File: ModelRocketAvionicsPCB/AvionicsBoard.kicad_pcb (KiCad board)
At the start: 4 copper layers, 30 x 55 mm, 67 parts, among them P1 FTSH-105-01-F-DV, P2 USB_OTG, P3 JST-2, U1 TM4C123GH6PM, U10 PMOS, U3 LIS331, U4 L3GD20HTR, U5 MPL3115A2, U6 MCP73831, U7 MIC5219-3.3BM5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

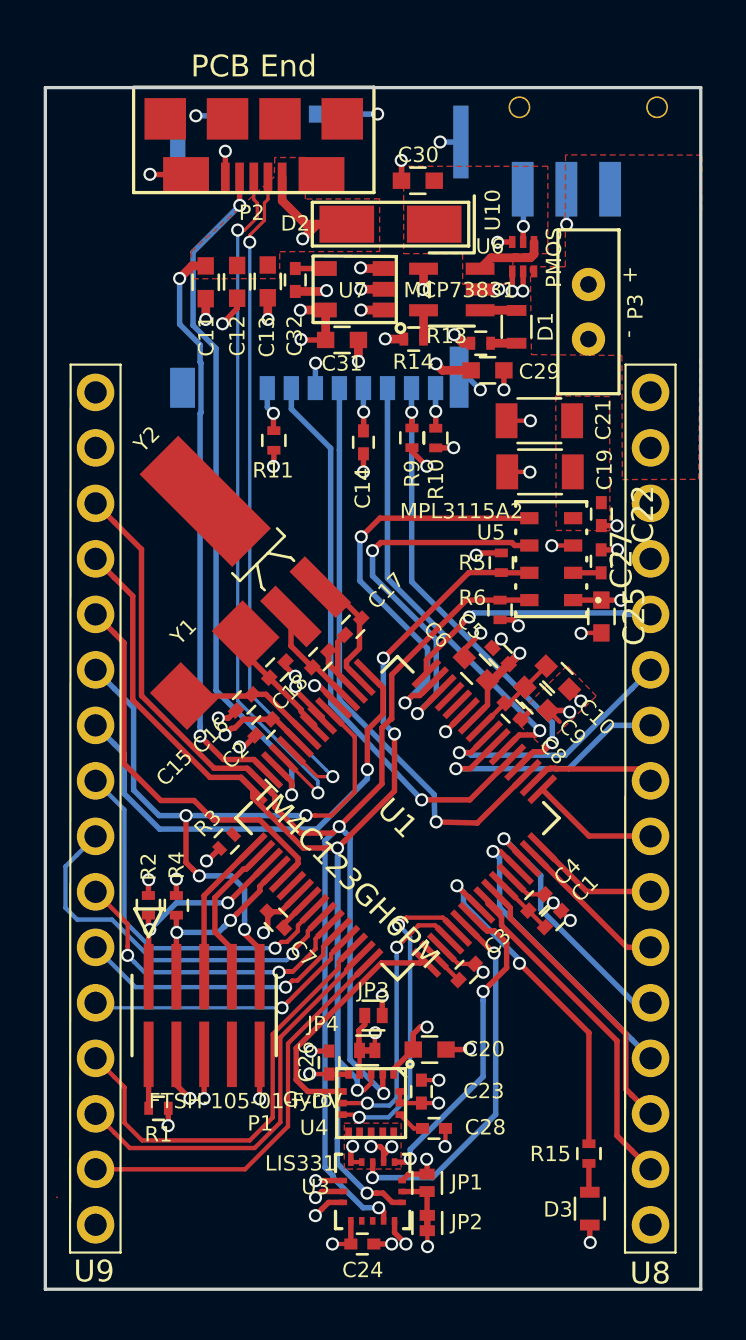
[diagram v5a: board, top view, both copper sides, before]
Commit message: DRC Issues Solved
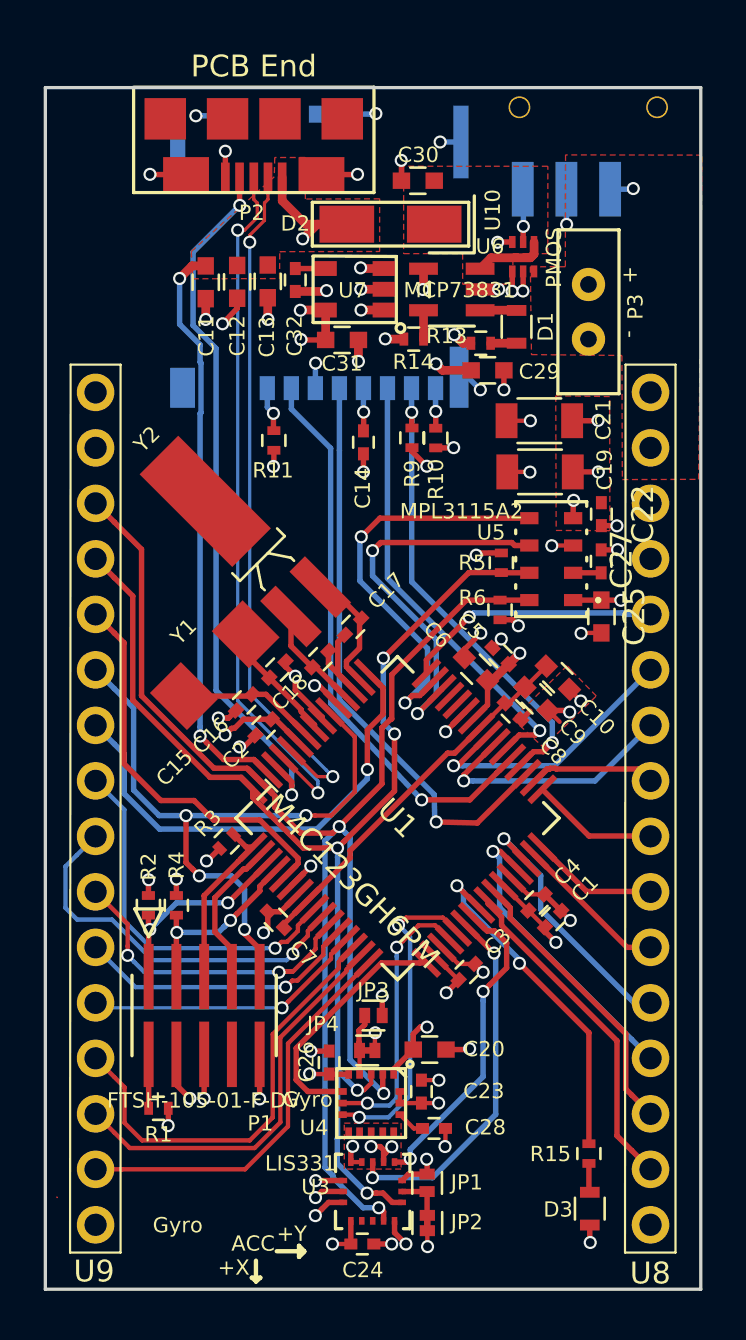
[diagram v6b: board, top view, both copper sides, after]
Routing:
- net PWR_VDDC: track 5.84 -> 17.3 mm
- net PB3/I2C_SDA: track 68.2 -> 58.6 mm
- net ACC_CS: track 42.7 -> 48.8 mm, vias 22 -> 28
- net PWR_GND: track 71.3 -> 73.9 mm, vias 59 -> 58
- net PC3/JTAG_TDO: track 6.85 -> 7.96 mm
- net +VBAT: track 0.00 -> 1.07 mm, vias 0 -> 1
- net PA7: track 12.1 -> 13.0 mm
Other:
- board text added: "+X"
- board text added: "+Y"
- board text added: "ACC"

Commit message: CDR Complete
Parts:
- R15: value 330 -> 100
- U10: value PMOS -> DMG1029SV-7
- moved D3 54.1 mm to (88.1, 76.8), turned to 270 degrees
- moved R15 49.5 mm to (88.2, 79.3), turned to 270 degrees
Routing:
- net PE1/IND_LED: track 15.8 -> 87.7 mm
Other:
- board text added: "Altimeter"
- board text added: "JTAG"
- board text added: "PMOS"

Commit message: Final Board REV 1a - Gerber Files
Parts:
- U11: renamed from Off U11 On; moved to F.Cu
- moved D3 0.56 mm to (88.2, 77.3)
- turned U11 to 180 degrees
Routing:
- net PWR_SWITCH: track 2.43 -> 10.3 mm, vias 1 -> 0
- net +VBAT: track 1.07 -> 0.00 mm, vias 1 -> 0
- net Net-(D3-Pad2): track 1.34 -> 0.76 mm
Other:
- board text added: "On Off"
- board text added: "SFU Rocketry Avionics REV 1a"
